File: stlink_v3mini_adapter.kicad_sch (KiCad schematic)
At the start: 15 parts, among them J1 Conn_02x07_Odd_Even, J2 Conn_02x05_Odd_Even, SW1 RST, U3 TLV71333PDBV

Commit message: add screws, switch to 2 layers
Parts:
- added D3: D_Schottky, Diode_SMD:D_SOD-523, symbol Device:D_Schottky
- added R3, R4: R, Resistor_SMD:R_0402_1005Metric, symbol Device:R
- F3: now not fitted
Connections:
- net +3.3V: now also R3.2
- net +BATT: now also R4.2
- net at F3.1, JP3.2 (B): now also R4.1
- net at C1.1, U2.22 (5V), U3.1 (IN)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: now also D3.2 (A); no longer F3.2
- net at F2.2, JP4.1 (A): now also R3.1
- new net: D3.1 (K), F3.2
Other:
- title: stlinkv3mini/mods wirestone adapter -> stlinkv3mods wirestone adapter
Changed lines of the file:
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@@
   (paper "A4")
   (title_block
-    (title "stlinkv3mini/mods wirestone adapter")
-    (date "2023-01-16")
+    (title "stlinkv3mods wirestone adapter")
+    (date "2023-01-24")
     (rev "1.0")
   )
+  (junction (at 193.04 120.65) (diameter 0) (color 0 0 0 0)
+  )
+  (junction (at 209.55 120.65) (diameter 0) (color 0 0 0 0)
+  )
   (junction (at 179.07 120.65) (diameter 0) (color 0 0 0 0)
   )
   (junction (at 213.36 90.17) (diameter 0) (color 0 0 0 0)
   )
+  (junction (at 207.01 90.17) (diameter 0) (color 0 0 0 0)
+  )
   (junction (at 156.21 123.19) (diameter 0) (color 0 0 0 0)
   )
@@
   )
   (junction (at 156.21 90.17) (diameter 0) (color 0 0 0 0)
+  )
+  (junction (at 196.85 90.17) (diameter 0) (color 0 0 0 0)
   )
   (no_connect (at 100.33 60.96))
@@
     (stroke (width 0) (type default))
   )
+  (wire (pts (xy 193.04 129.54) (xy 193.04 120.65))
+    (stroke (width 0) (type default))
+  )
   (wire (pts (xy 129.54 110.49) (xy 135.89 110.49))
     (stroke (width 0) (type default))
@@
     (stroke (width 0) (type default))
   )
-  (wire (pts (xy 184.15 90.17) (xy 156.21 90.17))
+  (wire (pts (xy 205.74 129.54) (xy 209.55 129.54))
+    (stroke (width 0) (type default))
+  )
+  (wire (pts (xy 193.04 120.65) (xy 196.85 120.65))
+    (stroke (width 0) (type default))
+  )
+  (wire (pts (xy 184.15 90.17) (xy 173.99 90.17))
     (stroke (width 0) (type default))
   )
@@
     (stroke (width 0) (type default))
   )
+  (wire (pts (xy 196.85 83.82) (xy 198.12 83.82))
+    (stroke (width 0) (type default))
+  )
   (wire (pts (xy 196.85 90.17) (xy 189.23 90.17))
     (stroke (width 0) (type default))
@@
     (stroke (width 0) (type default))
   )
-  (wire (pts (xy 207.01 120.65) (xy 213.36 120.65))
+  (wire (pts (xy 205.74 83.82) (xy 207.01 83.82))
+    (stroke (width 0) (type default))
+  )
+  (wire (pts (xy 207.01 120.65) (xy 209.55 120.65))
     (stroke (width 0) (type default))
   )
@@
     (stroke (width 0) (type default))
   )
+  (wire (pts (xy 193.04 129.54) (xy 198.12 129.54))
+    (stroke (width 0) (type default))
+  )
   (wire (pts (xy 179.07 130.81) (xy 179.07 134.62))
     (stroke (width 0) (type default))
@@
     (stroke (width 0) (type default))
   )
+  (wire (pts (xy 209.55 120.65) (xy 213.36 120.65))
+    (stroke (width 0) (type default))
+  )
   (wire (pts (xy 156.21 90.17) (xy 129.54 90.17))
     (stroke (width 0) (type default))
@@
     (stroke (width 0) (type default))
   )
+  (wire (pts (xy 196.85 83.82) (xy 196.85 90.17))
+    (stroke (width 0) (type default))
+  )
   (wire (pts (xy 123.19 48.26) (xy 129.54 48.26))
     (stroke (width 0) (type default))
@@
     (stroke (width 0) (type default))
   )
-  (wire (pts (xy 187.96 120.65) (xy 196.85 120.65))
+  (wire (pts (xy 166.37 90.17) (xy 156.21 90.17))
+    (stroke (width 0) (type default))
+  )
+  (wire (pts (xy 187.96 120.65) (xy 193.04 120.65))
     (stroke (width 0) (type default))
   )
@@
   )
   (wire (pts (xy 86.36 113.03) (xy 90.17 113.03))
+    (stroke (width 0) (type default))
+  )
+  (wire (pts (xy 209.55 129.54) (xy 209.55 120.65))
+    (stroke (width 0) (type default))
+  )
+  (wire (pts (xy 207.01 83.82) (xy 207.01 90.17))
     (stroke (width 0) (type default))
   )
@@
   )
   (symbol (lib_id "Device:Polyfuse_Small") (at 186.69 90.17 270) (mirror x) (unit 1)
-    (in_bom yes) (on_board yes) (dnp no)
+    (in_bom yes) (on_board yes) (dnp yes)
     (property "Reference" "F3" (at 146.05 93.98 90)
       (effects (font (size 1.27 1.27)) hide)
@@
         (path "/c9d8f4e4-9511-43ba-bbe3-ea21a129e315"
           (reference "JP4") (unit 1)
+        )
+      )
+    )
+  )
+  (symbol (lib_id "Device:R") (at 201.93 129.54 90) (unit 1)
+    (in_bom yes) (on_board yes) (dnp yes)
+    (property "Reference" "R3" (at 200.66 125.73 0)
+      (effects (font (size 1.27 1.27)) (justify left))
+    )
+    (property "Value" "R" (at 203.2 125.73 0)
+      (effects (font (size 1.27 1.27)) (justify left))
+    )
+    (property "Footprint" "Resistor_SMD:R_0402_1005Metric" (at 201.93 131.318 90)
+      (effects (font (size 1.27 1.27)) hide)
+    )
+    (property "Datasheet" "~" (at 201.93 129.54 0)
+      (effects (font (size 1.27 1.27)) hide)
+    )
+    (pin "1")
+    (pin "2")
+    (instances
+      (project "stlink_v3mini_adapter"
+        (path "/c9d8f4e4-9511-43ba-bbe3-ea21a129e315"
+          (reference "R3") (unit 1)
         )
       )
@@
         (path "/c9d8f4e4-9511-43ba-bbe3-ea21a129e315"
           (reference "C1") (unit 1)
+        )
+      )
+    )
+  )
+  (symbol (lib_id "Device:R") (at 201.93 83.82 90) (unit 1)
+    (in_bom yes) (on_board yes) (dnp yes)
+    (property "Reference" "R4" (at 200.66 80.01 0)
+      (effects (font (size 1.27 1.27)) (justify left))
+    )
+    (property "Value" "R" (at 203.2 80.01 0)
+      (effects (font (size 1.27 1.27)) (justify left))
+    )
+    (property "Footprint" "Resistor_SMD:R_0402_1005Metric" (at 201.93 85.598 90)
+      (effects (font (size 1.27 1.27)) hide)
+    )
+    (property "Datasheet" "~" (at 201.93 83.82 0)
+      (effects (font (size 1.27 1.27)) hide)
+    )
+    (pin "1")
+    (pin "2")
+    (instances
+      (project "stlink_v3mini_adapter"
+        (path "/c9d8f4e4-9511-43ba-bbe3-ea21a129e315"
+          (reference "R4") (unit 1)
         )
       )
@@
         )
       )
+    )
+  )
+  (symbol (lib_id "Device:D_Schottky") (at 170.18 90.17 180) (unit 1)
+    (in_bom yes) (on_board yes) (dnp yes) (fields_autoplaced)
+    (property "Reference" "D3" (at 170.4975 85.09 0)
+      (effects (font (size 1.27 1.27)))
+    )
+    (property "Value" "D_Schottky" (at 170.4975 87.63 0)
+      (effects (font (size 1.27 1.27)))
+    )
+    (property "Footprint" "Diode_SMD:D_SOD-523" (at 170.18 90.17 0)
+      (effects (font (size 1.27 1.27)))
+    )
+    (property "Datasheet" "~" (at 170.18 90.17 0)
+      (effects (font (size 1.27 1.27)) hide)
+    )
+    (pin "1")
+    (pin "2")
+    (instances
+      (project "stlink_v3mini_adapter"
+        (path "/c9d8f4e4-9511-43ba-bbe3-ea21a129e315"
+          (reference "D3") (unit 1)
+        )
+      )

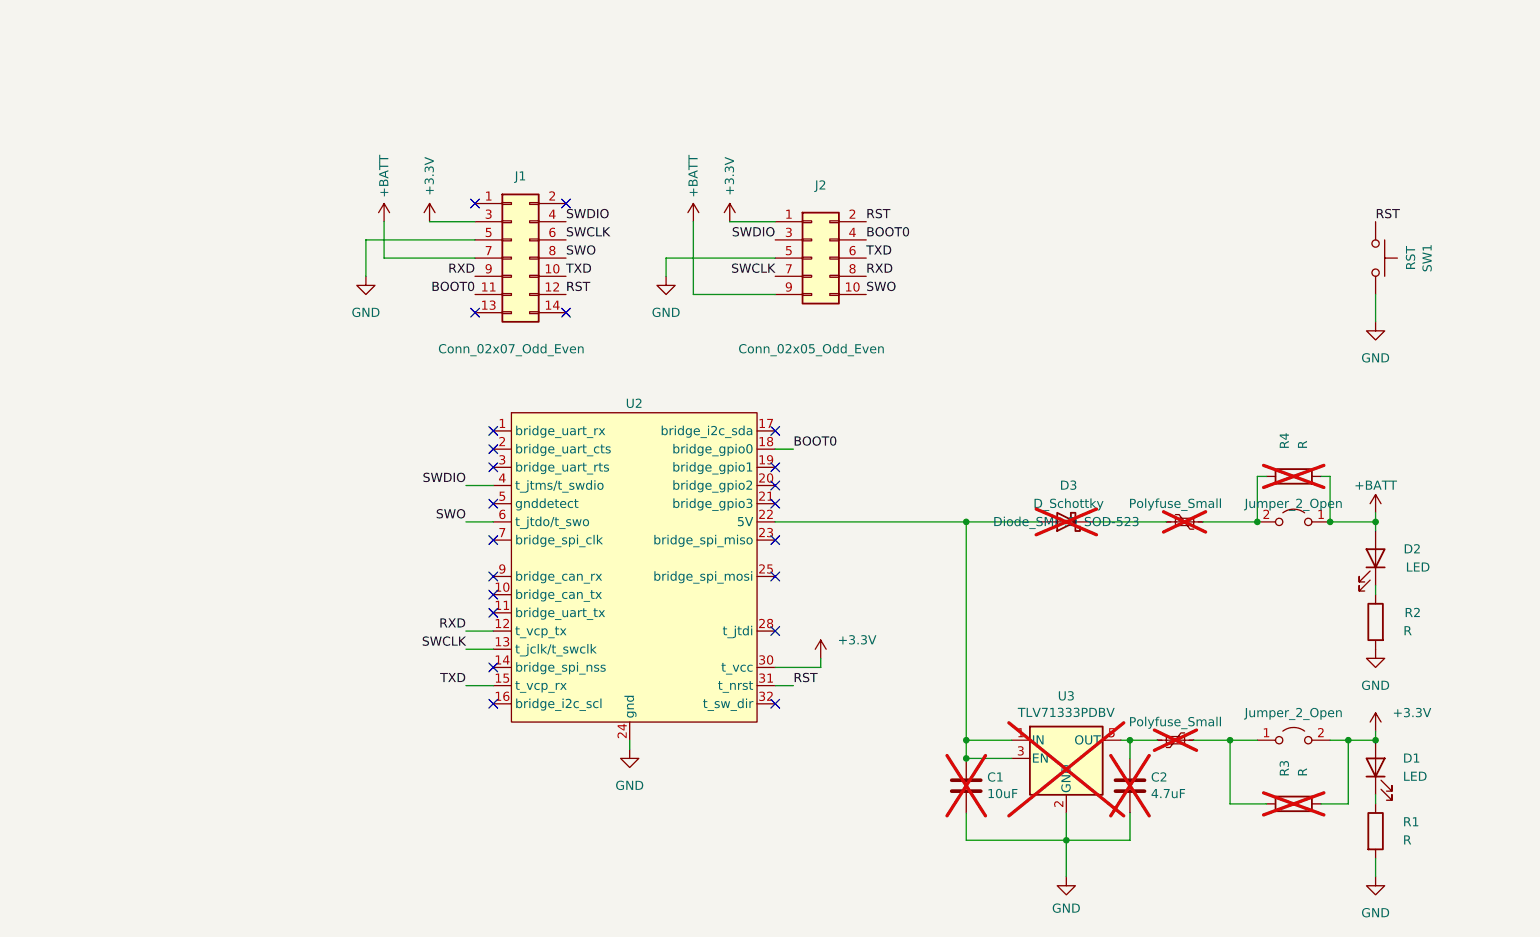
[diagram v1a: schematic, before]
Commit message: 1.1.0 with tx jumper
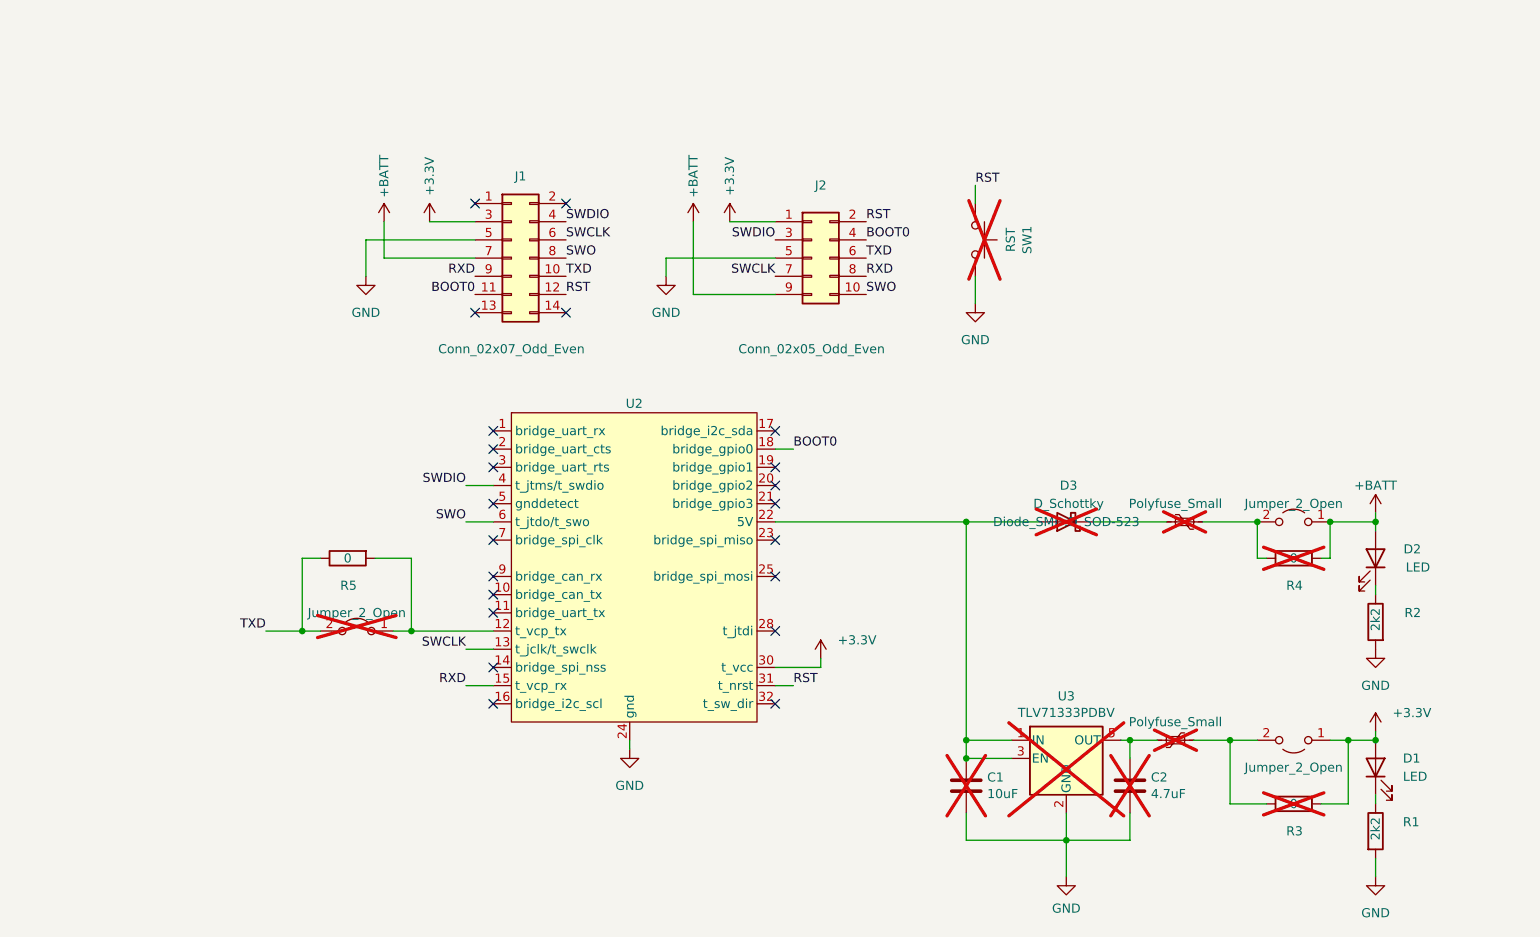
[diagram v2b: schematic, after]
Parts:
- added JP1: Jumper_2_Open, Connector_PinSocket_2.54mm:PinSocket_1x02_P2.54mm_Vertical, symbol Jumper:Jumper_2_Open
- added R5: 0, Resistor_SMD:R_0402_1005Metric, symbol Device:R
- F2, F3: footprint Fuse:Fuse_1210_3225Metric -> Fuse:Fuse_0805_2012Metric
- R1, R2: value R -> 2k2
- R3, R4: value R -> 0
- SW1: now not fitted
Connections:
- net +3.3V: now also JP4.1 (A); no longer JP4.2 (B)
- net RXD: now also U2.15 (t_vcp_rx); no longer U2.12 (t_vcp_tx)
- net TXD: now also JP1.2 (B), R5.1; no longer U2.15 (t_vcp_rx)
- net at F2.2, R3.1: now also JP4.2 (B); no longer JP4.1 (A)
- new net: JP1.1 (A), R5.2, U2.12 (t_vcp_tx)
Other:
- moved on the sheet: R4

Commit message: wip
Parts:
- added D4, D5, D6, D7, D8: PESD3V3L1BA, PCM_Diode_SMD_AKL:D_SOD-323_TVS, symbol PCM_Diode_TVS_AKL:PESD3V3L1BA
- added D9: D_Schottky, Diode_SMD:D_SOD-523, symbol Device:D_Schottky
- added R10, R6, R7, R8, R9: 100, Resistor_SMD:R_0402_1005Metric, symbol Device:R
- added R11: 2k2, Resistor_SMD:R_0402_1005Metric, symbol Device:R
- D1, D2: footprint LED_SMD:LED_0402_1005Metric -> LED_SMD:LED_0603_1608Metric
- J1: LCSC (none) -> C6332251
- J2: now not fitted
- R5: value 0 -> O
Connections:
- net GND: now also D4.1 (K), D5.1 (K), D6.1 (K), D7.1 (K), D8.1 (K)
- net RXD: now also D7.2 (A), R9.1; no longer U2.15 (t_vcp_rx)
- net SWCLK: now also D4.2 (A), R8.1; no longer U2.13 (t_jclk/t_swclk)
- net SWDIO: now also D6.2 (A), R6.1; no longer U2.4 (t_jtms/t_swdio)
- net SWO: now also D5.2 (A), R7.1; no longer U2.6 (t_jtdo/t_swo)
- net TXD: now also D8.2 (A)
- net at JP1.1 (A), R5.2: now also R10.1; no longer U2.12 (t_vcp_tx)
- net at C2.1, U3.5 (OUT): now also D9.2 (A); no longer F2.1
- net +5V: now reaches C1.1, D3.2 (A), U2.22 (5V), U3.1 (IN)
- net +5V: now also R11.1; no longer U3.3 (EN)
- net EN_3V3: now reaches U2.19 (bridge_gpio1)
- net EN_3V3: now also U3.3 (EN), R11.2
- new net: R10.2, U2.12 (t_vcp_tx)
- new net: R8.2, U2.13 (t_jclk/t_swclk)
- new net: R7.2, U2.6 (t_jtdo/t_swo)
- new net: D9.1 (K), F2.1
- new net: R9.2, U2.15 (t_vcp_rx)
- new net: R6.2, U2.4 (t_jtms/t_swdio)
- no-connect marks 22 -> 21
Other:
- moved on the sheet: C1, D1, J1, R1, R3, R5, SW1

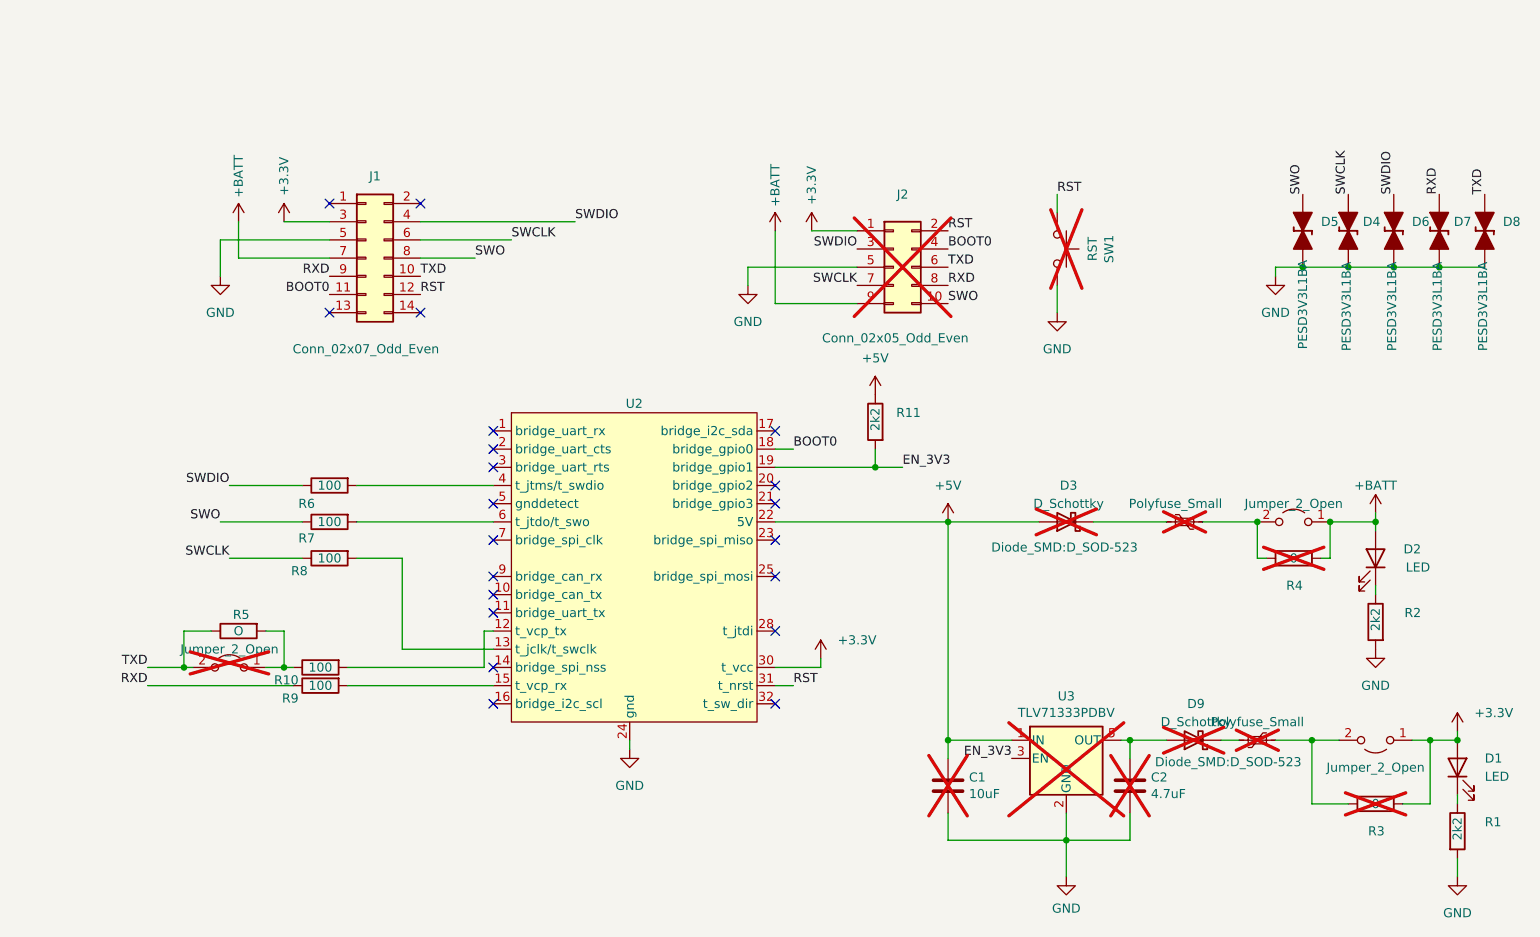
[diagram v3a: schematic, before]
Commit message: v1.2.0: add simple connector
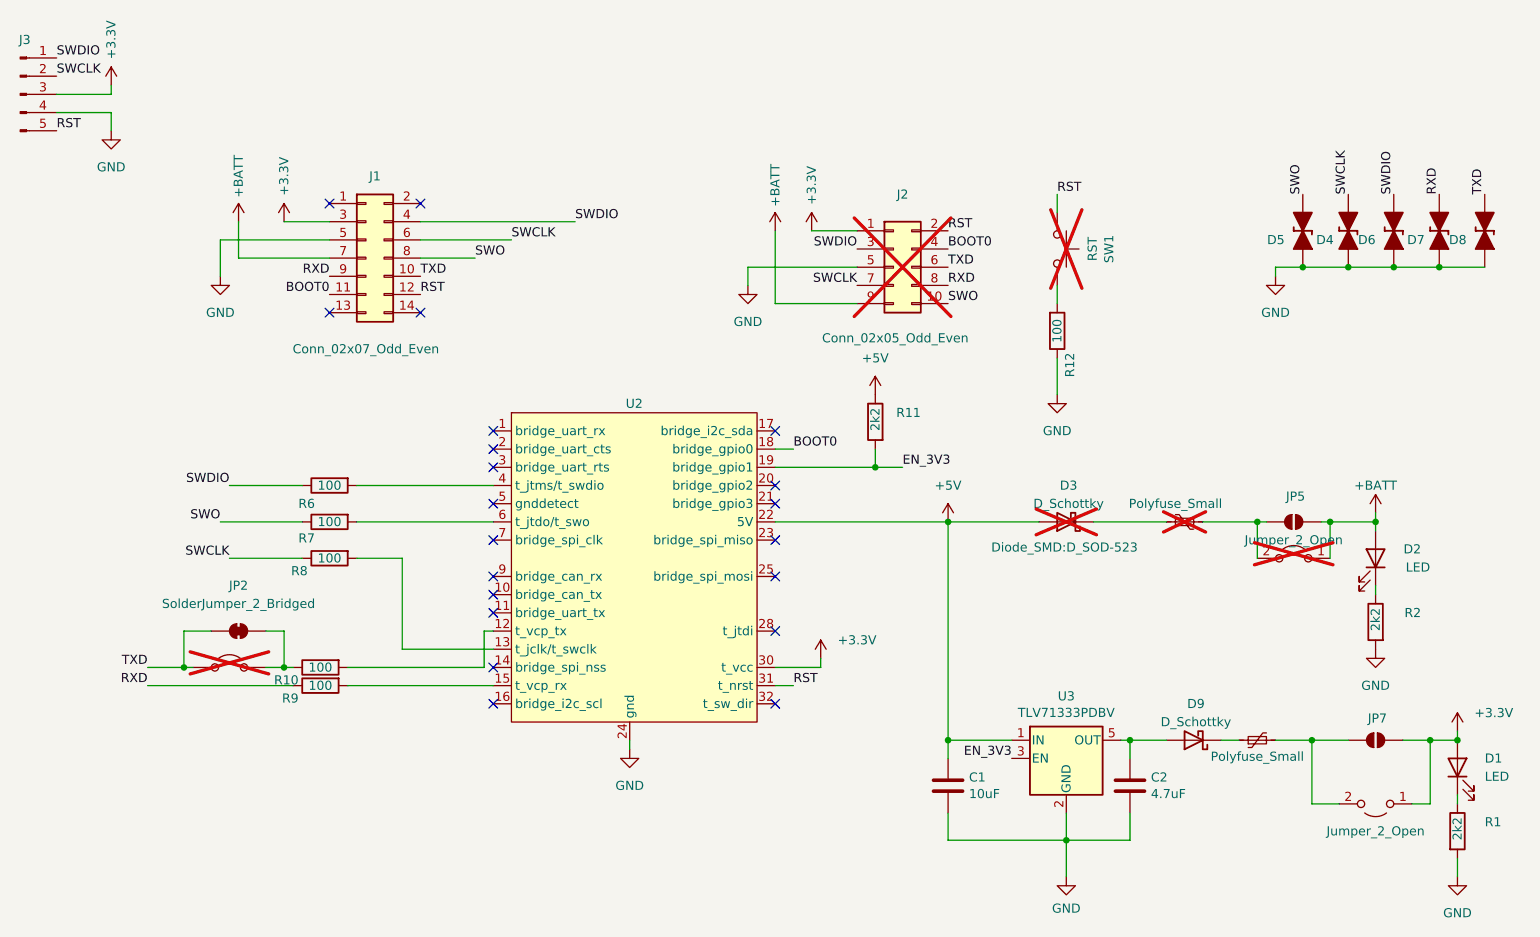
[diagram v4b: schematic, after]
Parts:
- removed R3, R4: 0, Resistor_SMD:R_0402_1005Metric, symbol Device:R
- removed R5: O, Resistor_SMD:R_0402_1005Metric, symbol Device:R
- added J3: Conn_01x05_Pin, Connector_PinHeader_2.54mm:PinHeader_1x05_P2.54mm_Vertical, symbol Connector:Conn_01x05_Pin
- added JP2: SolderJumper_2_Bridged, Jumper:SolderJumper-2_P1.3mm_Bridged_RoundedPad1.0x1.5mm, symbol Jumper:SolderJumper_2_Bridged
- added JP5, JP7: SolderJumper_2_Bridged, Jumper:SolderJumper-2_P1.3mm_Open_RoundedPad1.0x1.5mm, symbol Jumper:SolderJumper_2_Open
- added R12: 100, Resistor_SMD:R_0402_1005Metric, symbol Device:R
- C1, C2, D9, U3: now fitted
- D4, D5, D6, D7, D8: footprint PCM_Diode_SMD_AKL:D_SOD-323_TVS -> Resistor_SMD:R_0603_1608Metric
- F2: footprint Fuse:Fuse_0805_2012Metric -> Fuse:Fuse_0603_1608Metric; now fitted
- F3: footprint Fuse:Fuse_0805_2012Metric -> Fuse:Fuse_0603_1608Metric
- JP3: now not fitted
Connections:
- net +3.3V: now also J3.3 (Pin_3), JP7.2 (B)
- net +BATT: now also JP5.2 (B)
- net GND: now also D4.2 (A), D5.2 (A), D6.2 (A), D7.2 (A), D8.2 (A), J3.4 (Pin_4), R12.1; no longer D4.1 (K), D5.1 (K), D6.1 (K), D7.1 (K), D8.1 (K), SW1.2
- net RST: now also J3.5 (Pin_5)
- net RXD: now also D7.1 (K); no longer D7.2 (A)
- net SWCLK: now also D4.1 (K), J3.2 (Pin_2); no longer D4.2 (A)
- net SWDIO: now also D6.1 (K), J3.1 (Pin_1); no longer D6.2 (A)
- net SWO: now also D5.1 (K); no longer D5.2 (A)
- net TXD: now also D8.1 (K), JP2.1 (A); no longer D8.2 (A)
- net at JP1.1 (A), R10.1: now also JP2.2 (B)
- net at F3.1, JP3.2 (B): now also JP5.1 (A)
- net at F2.2, JP4.2 (B): now also JP7.1 (A)
- new net: R12.2, SW1.2
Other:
- moved on the sheet: D4, D5, D6, D7, D8
